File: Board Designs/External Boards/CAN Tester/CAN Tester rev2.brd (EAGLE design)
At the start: 83.8 x 100.3 mm, 30 parts, among them M1 Minifit-1, M2 Nanofit-1, M3 Nanofit-2, M4 Minifit-2, U1 ISOLATED CAN TRANSCIEVER, U3 TEENSY_3.2_SIMPLE, U4 CHARACTER_LCD

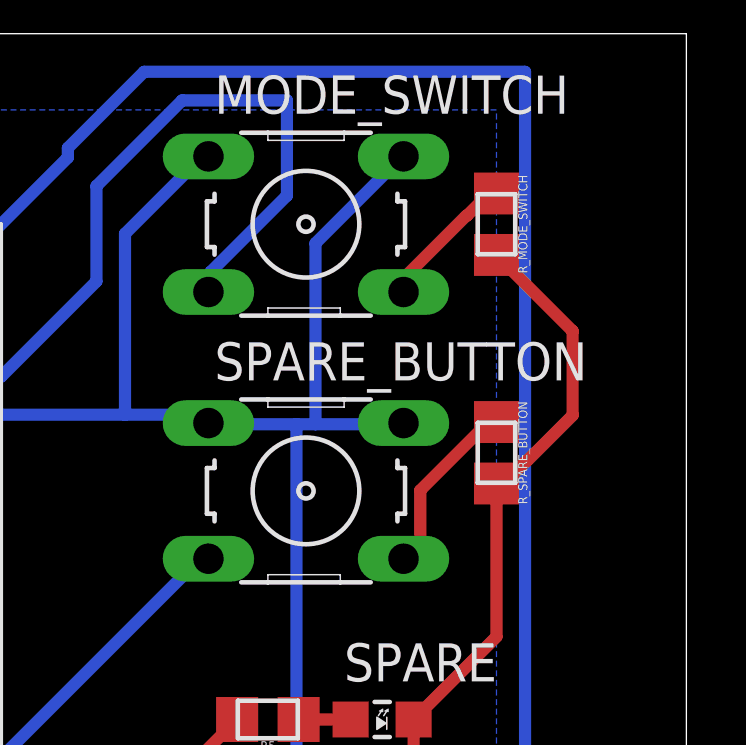
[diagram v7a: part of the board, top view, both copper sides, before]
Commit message: Adjusted traces for buttons on CAN_Tester
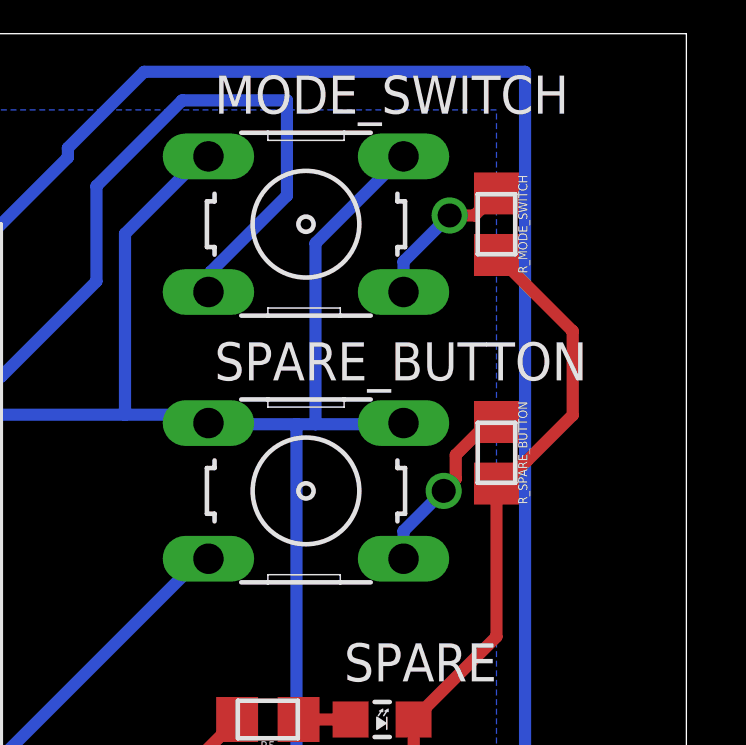
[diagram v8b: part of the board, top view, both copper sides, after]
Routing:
- net N$12: track 5.07 -> 5.30 mm, vias 0 -> 1
- net N$14: vias 0 -> 1
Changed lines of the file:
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@@
 <contactref element="MODE_SWITCH" pad="4"/>
 <contactref element="R_MODE_SWITCH" pad="1"/>
-<wire x1="76.46749375" y1="92.9946" x2="76.4846" y2="92.9946" width="0.4064" layer="1"/>
-<wire x1="76.4846" y1="92.9946" x2="77.47" y2="93.98" width="0.4064" layer="1"/>
-<wire x1="74.3712" y1="90.4494" x2="74.3712" y2="90.89830625" width="0.4064" layer="1"/>
-<wire x1="74.3712" y1="90.89830625" x2="76.46749375" y2="92.9946" width="0.4064" layer="1"/>
 <wire x1="77.47" y1="93.98" x2="77.47" y2="93.735" width="0.4064" layer="1"/>
+<wire x1="74.3712" y1="90.4494" x2="74.3712" y2="91.4639875" width="0.4064" layer="16"/>
+<wire x1="74.3712" y1="91.4639875" x2="75.90860625" y2="93.00139375" width="0.4064" layer="16"/>
+<via x="75.90860625" y="93.00139375" extent="1-16" drill="0.8" diameter="0.8"/>
+<wire x1="75.90860625" y1="93.00139375" x2="76.73639375" y2="93.00139375" width="0.4064" layer="1"/>
+<wire x1="76.73639375" y1="93.00139375" x2="77.47" y2="93.735" width="0.4064" layer="1"/>
 </signal>
 <signal name="N$14">
 <contactref element="SPARE_BUTTON" pad="4"/>
 <contactref element="R_SPARE_BUTTON" pad="1"/>
-<wire x1="74.3712" y1="81.5594" x2="74.93" y2="82.1182" width="0.4064" layer="1"/>
-<wire x1="74.93" y1="83.83710625" x2="77.20789375" y2="86.115" width="0.4064" layer="1"/>
-<wire x1="74.93" y1="82.1182" x2="74.93" y2="83.83710625" width="0.4064" layer="1"/>
 <wire x1="77.20789375" y1="86.115" x2="77.47" y2="86.115" width="0.4064" layer="1"/>
+<wire x1="74.3712" y1="81.5594" x2="74.3712" y2="82.4808" width="0.4064" layer="16"/>
+<wire x1="74.3712" y1="82.4808" x2="75.7104" y2="83.82" width="0.4064" layer="16"/>
+<via x="75.7104" y="83.82" extent="1-16" drill="0.8" diameter="0.8"/>
+<wire x1="75.7104" y1="83.82" x2="76.1104" y2="84.22" width="0.4064" layer="1"/>
+<wire x1="76.1104" y1="84.22" x2="76.1104" y2="85.01750625" width="0.4064" layer="1"/>
+<wire x1="76.1104" y1="85.01750625" x2="77.20789375" y2="86.115" width="0.4064" layer="1"/>
 </signal>
 <signal name="N$15">
